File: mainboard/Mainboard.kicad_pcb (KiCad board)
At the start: 4 copper layers, 106 x 80 mm, 135 parts, among them IC1001 TXB0104RUT, IC1002 PCA9306JK, IC1003 TXB0104RUT, IC1101 PCAL6416AHF, IC1102 TMP100, IC1103 RV-8263-C8, IC1104 PCA9633DP1,118, IC1201 TXB0102DCU, IC1202 PCA9306JK, IC506 PCA9306JK, IC602 USBLC6-2P6, IC701 BQ21040DBV, IC703 MAX17048, IC801 TPS62823DLC, IC802 LP5907MFX-2.8, IC803 LP5907MFX-1.5, IC804 LP5907MFX-3.0, IC805 LP5907MFX-2.8, IC806 LP5907MFX-1.2, M901 ESP32-S3-WROOM-1, Q1101 DMN2053UQ, Q1102 DMN2053UQ, Q701 PMV50XNEAR, X1001 LEPTON, X1201 Camera, X1301 Micro SD-Card, X1402 Displayboard, X701 USB, X901 Prog, Y1001 25 MHz, Y1201 25 MHz

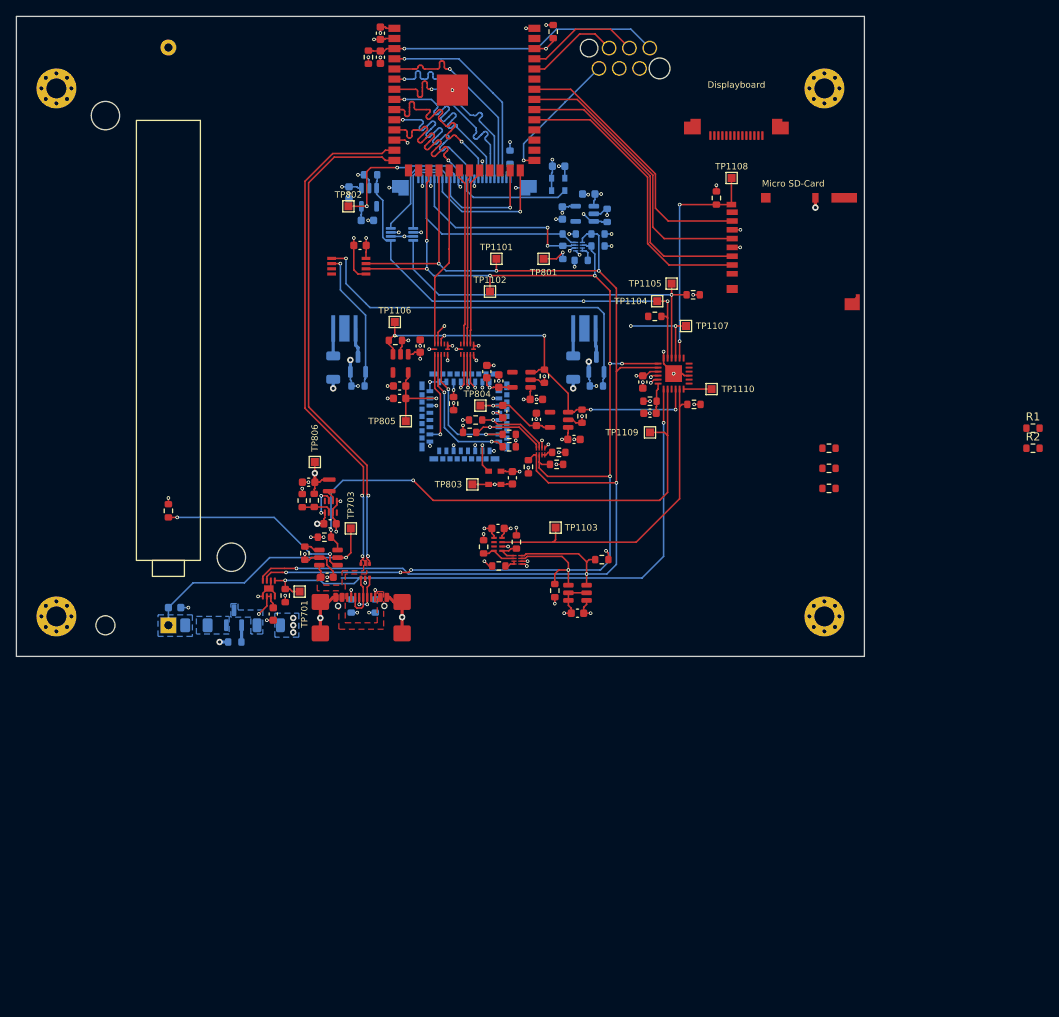
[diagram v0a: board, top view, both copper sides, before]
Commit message: Replace temperature sensor and optimize the position, replace LiPo battery with a flat one
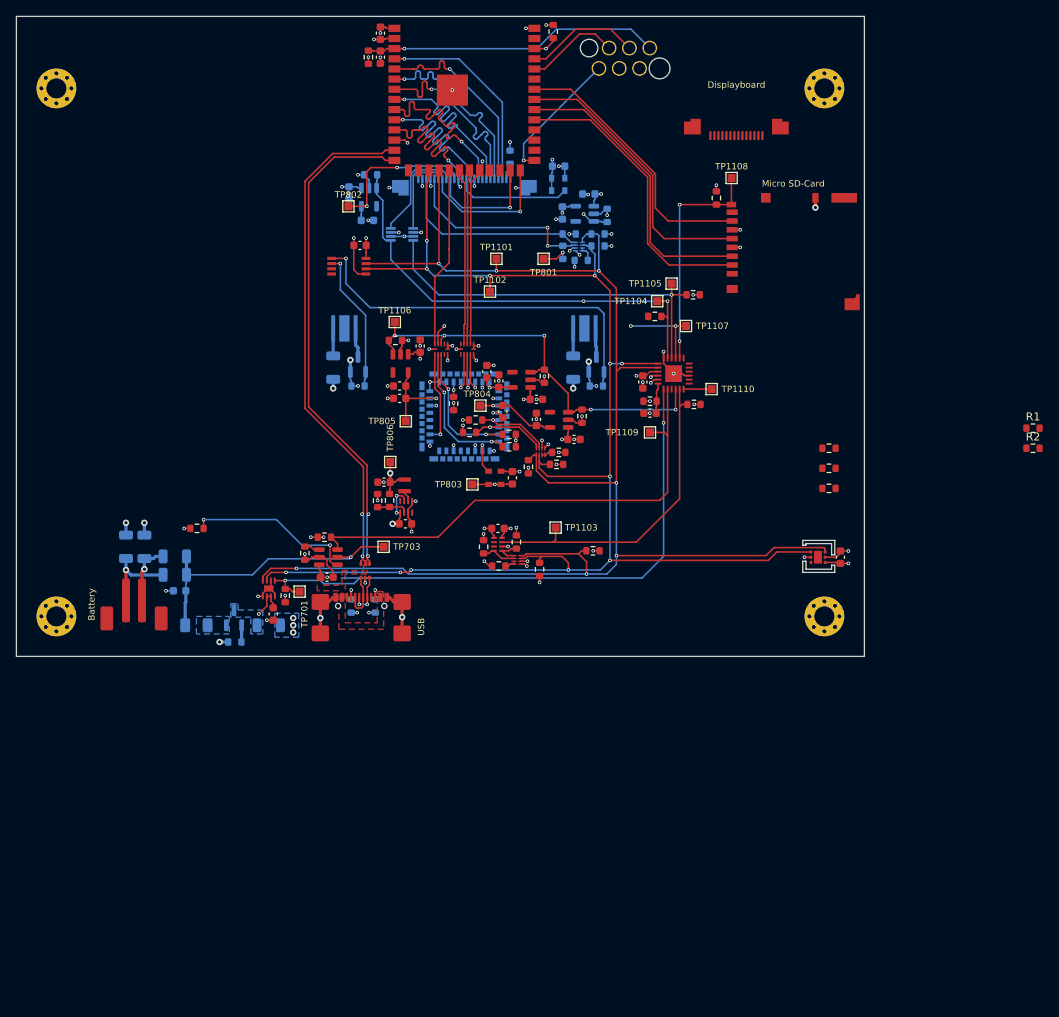
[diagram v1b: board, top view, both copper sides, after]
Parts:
- removed BT701: Battery, Battery_Kampi:Keystone_18650
- added R707: 0R, Resistor_SMD:R_1206_3216Metric, B.Cu at (171.8, 142.5)
- added R708: 0R, Resistor_SMD:R_1206_3216Metric, B.Cu at (171.8, 144.8)
- added R710: 0R, Resistor_SMD:R_1206_3216Metric, B.Cu at (168.0, 141.3)
- added R711: 0R, Resistor_SMD:R_1206_3216Metric, B.Cu at (165.7, 141.3)
- added X702: Battery, Connector_JST:JST_PH_B2B-PH-SM4-TB_1x02-1MP_P2.00mm_Vertical, F.Cu at (166.7, 148.5)
- IC1102: value TMP100 -> TMP117xxYBG; footprint Package_TO_SOT_SMD:SOT-23-6 -> Package_SON:WSON-6-1EP_2x2mm_P0.65mm_EP1x1.6mm
- moved C1103 33.6 mm to (255.0, 142.6), turned to -90 degrees
- moved IC1102 30.4 mm to (252.2, 142.6)
- moved L801 9.42 mm to (200.5, 133.6)
- moved R803 9.42 mm to (198.7, 135.5)
- moved R804 9.42 mm to (197.2, 135.5)
- moved C801 9.42 mm to (200.6, 138.4)
- moved C806 9.42 mm to (197.9, 133.2)
- moved IC801 9.42 mm to (200.7, 136.3)
- moved TP806 9.42 mm to (198.7, 130.7)
- moved TP703 4.70 mm to (197.9, 141.3), turned to -90 degrees
- moved TH701 4.20 mm to (174.6, 139.0), turned to 180 degrees
- moved R1108 3.26 mm to (217.4, 144.1)
- moved C702 2.19 mm to (172.4, 146.8), turned to 180 degrees
- moved R1109 1.56 mm to (224.1, 141.8)
- moved IC701 0.05 mm to (191.0, 142.6)
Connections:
- IC1102 pad 3: GND -> unconnected-(IC1102-ALERT-Pad3)
- IC1102 pad 4: +3V3 -> GND
- IC1102 pad 5: GND -> +3V3
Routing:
- net /Project Architecture/Battery/I2C-SDA: track 165.4 -> 190.9 mm, vias 6 -> 7
- net /Project Architecture/Battery/I2C-SCL: track 159.8 -> 181.2 mm, vias 11 -> 12
- net Net-(X702-Pin_2): track 0.00 -> 10.1 mm, vias 0 -> 1
- net Net-(X702-Pin_1): track 0.00 -> 7.81 mm, vias 0 -> 1
- net /Project Architecture/Battery/Battery-Charge: track 67.1 -> 61.6 mm, vias 2 -> 0
- net Net-(IC701-OUT): track 32.0 -> 36.4 mm
- net Net-(IC701-TS): track 24.1 -> 21.3 mm
- net GND: track 119.1 -> 119.3 mm, vias 73 -> 76
- removed copper zone on B.Cu, net Net-(IC701-OUT)
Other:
- outline, holes or cut-outs redrawn

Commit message: Layout complete
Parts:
- added R808: 100k, Resistor_SMD:R_0603_1608Metric, F.Cu at (219.2, 195.0)
- added SW701: On / Off, Button_Switch_THT:SW_Slide_SPDT_Angled_CK_OS102011MA1Q, F.Cu at (223.8, 195.7)
- F701: value 4 A -> 6 V / 4.5 A
- Q701: value PMV50XNEAR -> Si2333CDS; footprint Package_TO_SOT_SMD:SOT-23 -> Package_TO_SOT_SMD:SOT-23-3
- X702: footprint Connector_JST:JST_PH_B2B-PH-SM4-TB_1x02-1MP_P2.00mm_Vertical -> JST:S2B-PH-SM4-TB
- moved R1404 51.1 mm to (228.7, 120.2), turned to 90 degrees
- moved X1401 45.7 mm to (250.0, 132.0)
- moved C1103 44.8 mm to (263.0, 186.7)
- moved IC1102 44.8 mm to (260.2, 186.7)
- moved R1405 44.7 mm to (235.7, 137.5), turned to -90 degrees
- moved R1102 44.0 mm to (226.9, 120.2)
- moved R1301 43.8 mm to (247.5, 140.8)
- moved X1301 43.8 mm to (257.1, 147.5)
- moved F701 43.8 mm to (182.7, 194.1)
- moved C702 43.8 mm to (180.5, 189.8)
- moved IC1105 43.7 mm to (220.2, 184.0)
- moved R705 43.7 mm to (179.8, 185.5)
- moved R707 43.7 mm to (179.8, 187.8)
- moved IC801 43.7 mm to (208.7, 179.3)
- moved IC804 43.7 mm to (223.1, 163.4)
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- renumbered C1105 to C1104, C1104 to C1105, IC506 to IC1103, IC1103 to IC1105, IC602 to IC701, IC701 to IC702, R1111 to R1103, R1103 to R1105, R1112 to R1106, R1108 to R1107, R1109 to R1108, R1105 to R1109, R1106 to R1110, R1107 to R1111, R1110 to R1112, R1208 to R1202, R1207 to R1203, R1202 to R1204, R1203 to R1205, R1204 to R1206, R1205 to R1207, R1206 to R1208, R1403 to R1401, R1401 to R1402, R1402 to R1403, R2 to R1404, R1 to R1405, R707 to R705, R710 to R706, R708 to R707, R711 to R708, R705 to R709, R706 to R710, R709 to R711, R1007 to R901, R1008 to R902, R901 to R903, TP1104 to TP1103, TP1105 to TP1104, TP1106 to TP1105, TP1107 to TP1106, TP1108 to TP1107, TP1103 to TP1108, TP703 to TP701, TP701 to TP702, TP806 to TP803, TP803 to TP804, TP804 to TP805, TP805 to TP806, X1402 to X1401
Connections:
- F701 pad 2: Net-(Q701-S) -> Net-(Q701-D)
- IC1101 pad 22: /Project Architecture/MCU/~{Expander-INT} -> /Project Architecture/MCU/~{Expander-Int}
- IC801 pad 1: +BATT -> Net-(IC801-EN)
- M901 pad 24: /Project Architecture/Display/~{Touch-CS} -> /Project Architecture/Display/~{Touch-Reset}
- M901 pad 38: /Project Architecture/MCU/~{Expander-INT} -> /Project Architecture/Display/~{Display-Expander-Int}
- M901 pad 39: unconnected-(M901-IO1-Pad39) -> /Project Architecture/MCU/~{Expander-Int}
- Q701 pad 2: Net-(Q701-S) -> Net-(IC703-CELL)
- Q701 pad 3: Net-(IC703-CELL) -> Net-(Q701-D)
- R1006 pad 1: unconnected-(R1006-Pad1) -> +3V3
- R1102 pad 1: /Project Architecture/MCU/~{Expander-INT} -> /Project Architecture/MCU/~{Expander-Int}
- R1401 pad 1: unconnected-(R1403-Pad1) -> /Project Architecture/Display/~{Display-CS}
- R1402 pad 1: /Project Architecture/Display/~{Display-CS} -> /Project Architecture/Display/~{Touch-Reset}
- R1403 pad 1: /Project Architecture/Display/~{Display-Reset} -> /Project Architecture/Display/~{Touch-IRQ}
- R1404 pad 1: /Project Architecture/Display/~{Touch-CS} -> /Project Architecture/Display/~{Display-Expander-Int}
- R1404 pad 2: unconnected-(R2-Pad2) -> +3V3
- R1405 pad 1: /Project Architecture/Display/~{Touch-IRQ} -> /Project Architecture/Display/~{Display-Reset}
- R1405 pad 2: unconnected-(R1-Pad2) -> +3V3
- X1401 pad 1: +3V3 -> /Project Architecture/Display/Display-Backlight
- X1401 pad 10: unconnected-(X1402-Pin_10-Pad10) -> /Project Architecture/Battery/I2C-SDA
- X1401 pad 11: unconnected-(X1402-Pin_11-Pad11) -> /Project Architecture/Display/~{Touch-IRQ}
- X1401 pad 12: unconnected-(X1402-Pin_12-Pad12) -> /Project Architecture/Display/~{Touch-Reset}
- X1401 pad 13: unconnected-(X1402-Pin_13-Pad13) -> GND
- X1401 pad 14: unconnected-(X1402-Pin_14-Pad14) -> +3V3
- X1401 pad 2: GND -> /Project Architecture/Display/SPI-MISO
- X1401 pad 3: unconnected-(X1402-Pin_3-Pad3) -> /Project Architecture/Display/SPI-MOSI
- X1401 pad 4: unconnected-(X1402-Pin_4-Pad4) -> /Project Architecture/Display/~{Display-CS}
- X1401 pad 5: unconnected-(X1402-Pin_5-Pad5) -> /Project Architecture/Display/Display-DC
- X1401 pad 6: unconnected-(X1402-Pin_6-Pad6) -> /Project Architecture/Display/SPI-SCLK
- X1401 pad 7: unconnected-(X1402-Pin_7-Pad7) -> /Project Architecture/Display/~{Display-Reset}
- X1401 pad 8: unconnected-(X1402-Pin_8-Pad8) -> /Project Architecture/Display/~{Display-Expander-Int}
- X1401 pad 9: unconnected-(X1402-Pin_9-Pad9) -> /Project Architecture/Battery/I2C-SCL
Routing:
- net /Project Architecture/Display/Display-Backlight: track 0.00 -> 62.6 mm, vias 0 -> 4
- net /Project Architecture/Display/~{Display-Reset}: track 0.00 -> 52.3 mm, vias 0 -> 4
- net /Project Architecture/MCU/~{Expander-Int}: track 0.00 -> 51.9 mm, vias 0 -> 2
- net /Project Architecture/MCU/~{Expander-INT}: track 50.6 -> 0.00 mm, vias 2 -> 0
- net /Project Architecture/Display/Display-DC: track 0.00 -> 50.3 mm, vias 0 -> 4
- net /Project Architecture/Display/~{Touch-IRQ}: track 0.00 -> 48.9 mm, vias 0 -> 4
- net /Project Architecture/Display/~{Touch-Reset}: track 0.00 -> 47.9 mm, vias 0 -> 4
- net /Project Architecture/Display/~{Display-Expander-Int}: track 0.00 -> 35.6 mm, vias 0 -> 2
- net /Project Architecture/Display/~{Display-CS}: track 0.00 -> 34.5 mm
- net Net-(IC801-EN): track 0.00 -> 25.8 mm
- net /Project Architecture/Battery/I2C-SCL: track 181.2 -> 205.0 mm, vias 12 -> 13
- net /Project Architecture/Battery/I2C-SDA: track 190.9 -> 213.1 mm, vias 7 -> 8
- net /Project Architecture/Display/SPI-MISO: track 34.1 -> 51.7 mm, vias 0 -> 2
- net /Project Architecture/Display/SPI-MOSI: track 37.2 -> 54.3 mm, vias 0 -> 2
- net /Project Architecture/Display/SPI-SCLK: track 35.8 -> 50.1 mm, vias 0 -> 2
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- added copper zone on B.Cu, net Net-(Q701-D)
- removed copper zone on B.Cu, net Net-(Q701-S)
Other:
- outline, holes or cut-outs redrawn

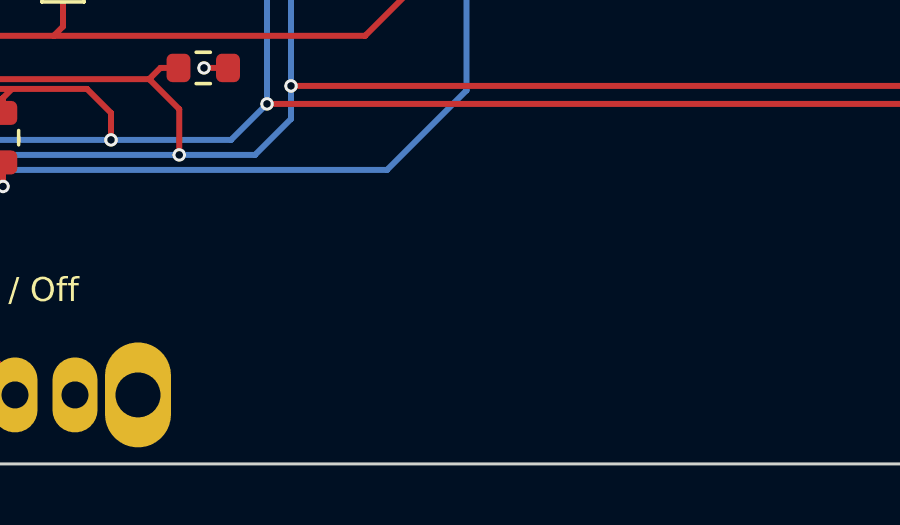
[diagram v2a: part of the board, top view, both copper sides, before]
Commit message: Add reset switch
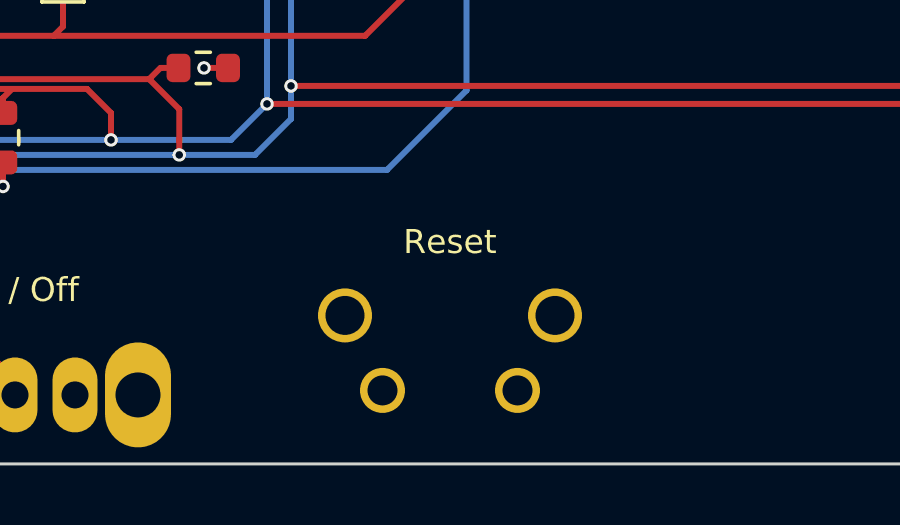
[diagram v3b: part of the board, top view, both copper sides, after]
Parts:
- added SW901: Reset, Same Sky:TS11, F.Cu at (240.3, 194.3)
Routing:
- net /Project Architecture/MCU/ESP-Enable: track 37.3 -> 131.6 mm

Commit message: Release 1.0.0
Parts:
- TP1101, TP1102, TP1103, TP1104, TP1105, TP1106, TP1107, TP1108, TP1109, TP1110, TP701, TP702, TP801, TP802, TP803, TP804, TP805, TP806: footprint TestPoint:TestPoint_Pad_1.0x1.0mm -> Testpoints_Kampi:TestPoint_Pad_1.0x1.0mm
- X901: moved to B.Cu
- moved X901 1.24 mm to (236.6, 123.3), turned to 180 degrees
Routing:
- net /Project Architecture/MCU/ESP-Boot: track 16.8 -> 21.8 mm
- net /Project Architecture/MCU/ESP-RxD: track 13.6 -> 18.4 mm, vias 0 -> 2
- net /Project Architecture/MCU/ESP-TxD: track 15.7 -> 12.4 mm
- net /Project Architecture/Display/~{Display-Expander-Int}: track 35.6 -> 37.1 mm
